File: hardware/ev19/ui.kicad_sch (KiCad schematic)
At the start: 43 parts, among them CN3 BM14B(0.8)-24DS-0.4V(53), J14 Conn_01x18_MountingPin, Q5 2N7002, SW4 SW_Push, SW5 SW_Push, SW6 SW_Push, SW7 SW_Push, U10 STM32F405RGTx

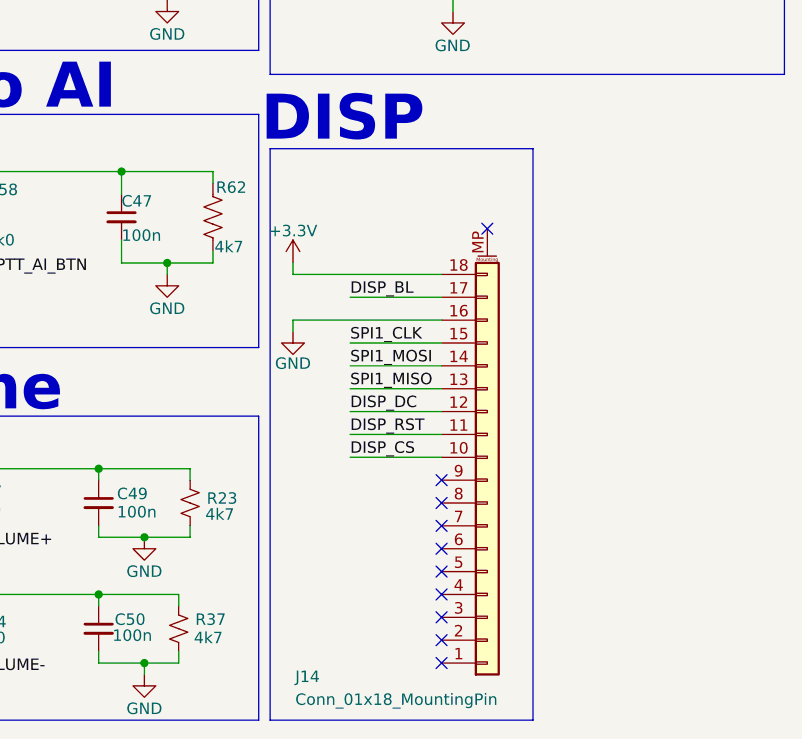
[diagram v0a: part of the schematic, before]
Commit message: wip- laid out the analog power section, added screen cut outs, decided on positions
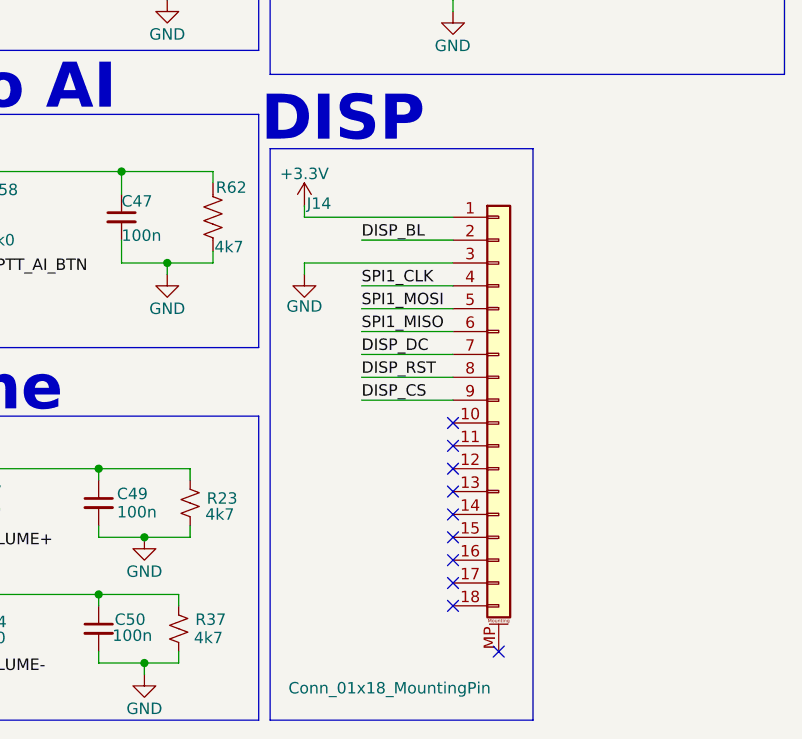
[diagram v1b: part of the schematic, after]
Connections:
- net +3.3V: now also J14.1 (Pin_1); no longer J14.18 (Pin_18)
- net DISP_BL: now also J14.2 (Pin_2); no longer J14.17 (Pin_17)
- net DISP_CS: now also J14.9 (Pin_9); no longer J14.10 (Pin_10)
- net DISP_DC: now also J14.7 (Pin_7); no longer J14.12 (Pin_12)
- net DISP_RST: now also J14.8 (Pin_8); no longer J14.11 (Pin_11)
- net GND: now also J14.3 (Pin_3); no longer J14.16 (Pin_16)
- net SPI1_CLK: now also J14.4 (Pin_4); no longer J14.15 (Pin_15)
- net SPI1_MISO: now also J14.6 (Pin_6); no longer J14.13 (Pin_13)
- net SPI1_MOSI: now also J14.5 (Pin_5); no longer J14.14 (Pin_14)
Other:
- moved on the sheet: J14
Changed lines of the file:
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@@
 	)
 	(no_connect
-		(at 245.11 147.32)
+		(at 246.38 140.97)
 	)
 	(no_connect
-		(at 245.11 142.24)
+		(at 246.38 135.89)
 	)
 	(no_connect
-		(at 245.11 139.7)
+		(at 246.38 133.35)
 	)
 	(no_connect
@@
 	)
 	(no_connect
-		(at 250.19 109.22)
+		(at 251.46 156.21)
 	)
 	(no_connect
-		(at 245.11 157.48)
+		(at 246.38 151.13)
 	)
 	(no_connect
-		(at 245.11 154.94)
+		(at 246.38 148.59)
 	)
 	(no_connect
-		(at 245.11 152.4)
+		(at 246.38 146.05)
 	)
 	(no_connect
-		(at 245.11 144.78)
+		(at 246.38 138.43)
 	)
 	(no_connect
@@
 	)
 	(no_connect
-		(at 245.11 137.16)
+		(at 246.38 130.81)
 	)
 	(no_connect
-		(at 245.11 149.86)
+		(at 246.38 143.51)
 	)
 	(wire
@@
 	(wire
 		(pts
-			(xy 234.95 121.92) (xy 245.11 121.92)
+			(xy 236.22 115.57) (xy 246.38 115.57)
 		)
 		(stroke
@@
 	(wire
 		(pts
-			(xy 228.6 119.38) (xy 245.11 119.38)
+			(xy 229.87 113.03) (xy 246.38 113.03)
 		)
 		(stroke
@@
 	(wire
 		(pts
-			(xy 234.95 132.08) (xy 245.11 132.08)
+			(xy 236.22 125.73) (xy 246.38 125.73)
 		)
 		(stroke
@@
 	(wire
 		(pts
-			(xy 228.6 113.03) (xy 228.6 114.3)
+			(xy 229.87 106.68) (xy 229.87 107.95)
 		)
 		(stroke
@@
 	(wire
 		(pts
-			(xy 228.6 120.65) (xy 228.6 119.38)
+			(xy 229.87 114.3) (xy 229.87 113.03)
 		)
 		(stroke
@@
 	(wire
 		(pts
-			(xy 234.95 134.62) (xy 245.11 134.62)
+			(xy 236.22 128.27) (xy 246.38 128.27)
 		)
 		(stroke
@@
 	(wire
 		(pts
-			(xy 234.95 129.54) (xy 245.11 129.54)
+			(xy 236.22 123.19) (xy 246.38 123.19)
 		)
 		(stroke
@@
 	(wire
 		(pts
-			(xy 228.6 114.3) (xy 245.11 114.3)
+			(xy 229.87 107.95) (xy 246.38 107.95)
 		)
 		(stroke
@@
 	(wire
 		(pts
-			(xy 234.95 116.84) (xy 245.11 116.84)
+			(xy 236.22 110.49) (xy 246.38 110.49)
 		)
 		(stroke
@@
 	(wire
 		(pts
-			(xy 234.95 127) (xy 245.11 127)
+			(xy 236.22 120.65) (xy 246.38 120.65)
 		)
 		(stroke
@@
 	(wire
 		(pts
-			(xy 234.95 124.46) (xy 245.11 124.46)
+			(xy 236.22 118.11) (xy 246.38 118.11)
 		)
 		(stroke
@@
 	)
 	(label "SPI1_MISO"
-		(at 234.95 127 0)
+		(at 236.22 120.65 0)
 		(effects
 			(font
@@
 	)
 	(label "DISP_CS"
-		(at 234.95 134.62 0)
+		(at 236.22 128.27 0)
 		(effects
 			(font
@@
 	)
 	(label "SPI1_MOSI"
-		(at 234.95 124.46 0)
+		(at 236.22 118.11 0)
 		(effects
 			(font
@@
 	)
 	(label "DISP_DC"
-		(at 234.95 129.54 0)
+		(at 236.22 123.19 0)
 		(effects
 			(font
@@
 	)
 	(label "DISP_RST"
-		(at 234.95 132.08 0)
+		(at 236.22 125.73 0)
 		(effects
 			(font
@@
 	)
 	(label "SPI1_CLK"
-		(at 234.95 121.92 0)
+		(at 236.22 115.57 0)
 		(effects
 			(font
@@
 	)
 	(label "DISP_BL"
-		(at 234.95 116.84 0)
+		(at 236.22 110.49 0)
 		(effects
 			(font
@@
 	(symbol
 		(lib_id "power:GND")
-		(at 228.6 120.65 0)
+		(at 229.87 114.3 0)
 		(unit 1)
 		(body_style 1)
@@
 		(dnp no)
 		(property "Reference" "#PWR0109"
-			(at 228.6 127 0)
+			(at 229.87 120.65 0)
 			(hide yes)
 			(show_name no)
@@
 		)
 		(property "Value" "GND"
-			(at 228.6 124.206 0)
+			(at 229.87 117.856 0)
 			(show_name no)
 			(do_not_autoplace no)
@@
 		)
 		(property "Footprint" ""
-			(at 228.6 120.65 0)
+			(at 229.87 114.3 0)
 			(hide yes)
 			(show_name no)
@@
 		)
 		(property "Datasheet" ""
-			(at 228.6 120.65 0)
+			(at 229.87 114.3 0)
 			(hide yes)
 			(show_name no)
@@
 		)
 		(property "Description" "Power symbol creates a global label with name \"GND\" , ground"
-			(at 228.6 120.65 0)
+			(at 229.87 114.3 0)
 			(hide yes)
 			(show_name no)
@@
 	(symbol
 		(lib_id "Connector_Generic_MountingPin:Conn_01x18_MountingPin")
-		(at 250.19 137.16 0)
-		(mirror x)
+		(at 251.46 128.27 0)
 		(unit 1)
 		(body_style 1)
@@
 		(dnp no)
 		(property "Reference" "J14"
-			(at 228.854 159.004 0)
+			(at 230.124 106.426 0)
 			(show_name no)
 			(do_not_autoplace no)
@@
 		)
 		(property "Value" "Conn_01x18_MountingPin"
-			(at 228.854 161.544 0)
+			(at 228.092 160.274 0)
 			(show_name no)
 			(do_not_autoplace no)
@@
 		)
 		(property "Footprint" "Connector_FFC-FPC:Hirose_FH12-18S-0.5SH_1x18-1MP_P0.50mm_Horizontal"
-			(at 250.19 137.16 0)
+			(at 251.46 128.27 0)
 			(hide yes)
 			(show_name no)
@@
 		)
 		(property "Datasheet" ""
-			(at 250.19 137.16 0)
+			(at 251.46 128.27 0)
 			(hide yes)
 			(show_name no)
@@
 		)
 		(property "Description" "Generic connectable mounting pin connector, single row, 01x18, script generated (kicad-library-utils/schlib/autogen/connector/)"
-			(at 250.19 137.16 0)
+			(at 251.46 128.27 0)
 			(hide yes)
 			(show_name no)
@@
 		)
 		(property "JLCPCB Part #" "C2856802"
-			(at 250.19 137.16 0)
+			(at 251.46 128.27 0)
 			(hide yes)
 			(show_name no)
@@
 	(symbol
 		(lib_id "power:+3.3V")
-		(at 228.6 113.03 0)
+		(at 229.87 106.68 0)
 		(unit 1)
 		(body_style 1)
@@
 		(dnp no)
 		(property "Reference" "#PWR0108"
-			(at 228.6 116.84 0)
+			(at 229.87 110.49 0)
 			(hide yes)
 			(show_name no)
@@
 		)
 		(property "Value" "+3.3V"
-			(at 228.6 109.474 0)
+			(at 229.87 103.124 0)
 			(show_name no)
 			(do_not_autoplace no)
@@
 		)
 		(property "Footprint" ""
-			(at 228.6 113.03 0)
+			(at 229.87 106.68 0)
 			(hide yes)
 			(show_name no)
@@
 		)
 		(property "Datasheet" ""
-			(at 228.6 113.03 0)
+			(at 229.87 106.68 0)
 			(hide yes)
 			(show_name no)
@@
 		)
 		(property "Description" "Power symbol creates a global label with name \"+3.3V\""
-			(at 228.6 113.03 0)
+			(at 229.87 106.68 0)
 			(hide yes)
 			(show_name no)

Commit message: Laid out all high speed lines, created gnda, 3.0va, and dgnd 3.3vd in analog sections
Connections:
- net MIC_IO renamed MIC_PTT_BTN
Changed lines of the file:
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@@
-	(wire
-		(pts
-			(xy 73.66 54.61) (xy 87.63 54.61)
-		)
-		(stroke
-			(width 0)
-			(type default)
-		)
-	)
 	(wire
 		(pts
@@
 		(pts
 			(xy 191.77 158.75) (xy 191.77 156.21)
+		)
+		(stroke
+			(width 0)
+			(type default)
+		)
+	)
+	(wire
+		(pts
+			(xy 46.99 54.61) (xy 87.63 54.61)
 		)
 		(stroke
@@
 	(label "SPI1_CLK"
 		(at 73.66 57.15 0)
-		(effects
-			(font
-				(size 1.27 1.27)
-			)
-			(justify left bottom)
-		)
-	)
-	(label "MIC_IO"
-		(at 73.66 54.61 0)
 		(effects
 			(font
@@
 		(effects
 			(font
+				(size 1.27 1.27)
+			)
+			(justify right)
+		)
+	)
+	(hierarchical_label "MIC_PTT_BTN"
+		(shape input)
+		(at 46.99 54.61 180)
+		(effects
+			(font

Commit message: Change connector for display, but will need to change footprint
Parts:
- removed J14: Conn_01x18_MountingPin, Connector_FFC-FPC:Hirose_FH12-18S-0.5SH_1x18-1MP_P0.50mm_Horizontal, symbol Connector_Generic_MountingPin:Conn_01x18_MountingPin
- added J13: Conn_01x08_Pin, Connector_PinHeader_2.54mm:PinHeader_1x08_P2.54mm_Vertical_SMD_Pin1Left, symbol Connector:Conn_01x08_Pin
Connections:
- net +3.3V: now also J13.8 (Pin_8)
- net DISP_BL: now also J13.1 (Pin_1)
- net DISP_CS: now also J13.4 (Pin_4)
- net DISP_DC: now also J13.3 (Pin_3)
- net DISP_RST: now also J13.2 (Pin_2)
- net GND: now also J13.7 (Pin_7)
- net SPI1_CLK: now also J13.5 (Pin_5)
- net SPI1_MOSI: now also J13.6 (Pin_6)
- no-connect marks 12 -> 2
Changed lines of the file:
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@@
 	)
 	(no_connect
-		(at 246.38 140.97)
-	)
-	(no_connect
-		(at 246.38 135.89)
-	)
-	(no_connect
-		(at 246.38 133.35)
-	)
-	(no_connect
 		(at 245.11 40.64)
 	)
 	(no_connect
-		(at 251.46 156.21)
-	)
-	(no_connect
-		(at 246.38 151.13)
-	)
-	(no_connect
-		(at 246.38 148.59)
-	)
-	(no_connect
-		(at 246.38 146.05)
-	)
-	(no_connect
-		(at 246.38 138.43)
-	)
-	(no_connect
 		(at 128.27 57.15)
 	)
-	(no_connect
-		(at 246.38 130.81)
-	)
-	(no_connect
-		(at 246.38 143.51)
-	)
 	(wire
 		(pts
@@
 	(wire
 		(pts
-			(xy 229.87 113.03) (xy 246.38 113.03)
+			(xy 229.87 110.49) (xy 246.38 110.49)
 		)
 		(stroke
@@
 	(wire
 		(pts
-			(xy 236.22 125.73) (xy 246.38 125.73)
+			(xy 236.22 123.19) (xy 246.38 123.19)
 		)
 		(stroke
@@
 	(wire
 		(pts
-			(xy 229.87 114.3) (xy 229.87 113.03)
+			(xy 229.87 111.76) (xy 229.87 110.49)
 		)
 		(stroke
@@
 	(wire
 		(pts
-			(xy 236.22 128.27) (xy 246.38 128.27)
+			(xy 236.22 118.11) (xy 246.38 118.11)
 		)
 		(stroke
@@
 	(wire
 		(pts
-			(xy 236.22 123.19) (xy 246.38 123.19)
+			(xy 236.22 120.65) (xy 246.38 120.65)
 		)
 		(stroke
@@
 	(wire
 		(pts
-			(xy 236.22 110.49) (xy 246.38 110.49)
+			(xy 236.22 125.73) (xy 246.38 125.73)
 		)
 		(stroke
@@
 	(wire
 		(pts
-			(xy 236.22 120.65) (xy 246.38 120.65)
-		)
-		(stroke
-			(width 0)
-			(type default)
-		)
-	)
-	(wire
-		(pts
 			(xy 128.27 92.71) (xy 160.02 92.71)
 		)
@@
 	(wire
 		(pts
-			(xy 236.22 118.11) (xy 246.38 118.11)
+			(xy 236.22 113.03) (xy 246.38 113.03)
 		)
 		(stroke
@@
 		)
 	)
-	(label "SPI1_MISO"
-		(at 236.22 120.65 0)
-		(effects
-			(font
-				(size 1.27 1.27)
-			)
-			(justify left bottom)
-		)
-	)
 	(label "SPI1_MOSI"
 		(at 73.66 62.23 0)
@@
 	)
 	(label "DISP_CS"
-		(at 236.22 128.27 0)
+		(at 236.22 118.11 0)
 		(effects
 			(font
@@
 	)
 	(label "SPI1_MOSI"
-		(at 236.22 118.11 0)
+		(at 236.22 113.03 0)
 		(effects
 			(font
@@
 	)
 	(label "DISP_DC"
-		(at 236.22 123.19 0)
+		(at 236.22 120.65 0)
 		(effects
 			(font
@@
 	)
 	(label "DISP_RST"
-		(at 236.22 125.73 0)
+		(at 236.22 123.19 0)
 		(effects
 			(font
@@
 	)
 	(label "DISP_BL"
-		(at 236.22 110.49 0)
+		(at 236.22 125.73 0)
 		(effects
 			(font
@@
 	(symbol
 		(lib_id "power:GND")
-		(at 229.87 114.3 0)
+		(at 229.87 111.76 0)
 		(unit 1)
 		(body_style 1)
@@
 		(dnp no)
 		(property "Reference" "#PWR0109"
-			(at 229.87 120.65 0)
+			(at 229.87 118.11 0)
 			(hide yes)
 			(show_name no)
@@
 		)
 		(property "Value" "GND"
-			(at 229.87 117.856 0)
+			(at 229.87 115.316 0)
 			(show_name no)
 			(do_not_autoplace no)
@@
 		)
 		(property "Footprint" ""
-			(at 229.87 114.3 0)
+			(at 229.87 111.76 0)
 			(hide yes)
 			(show_name no)
@@
 		)
 		(property "Datasheet" ""
-			(at 229.87 114.3 0)
+			(at 229.87 111.76 0)
 			(hide yes)
 			(show_name no)
@@
 		)
 		(property "Description" "Power symbol creates a global label with name \"GND\" , ground"
-			(at 229.87 114.3 0)
+			(at 229.87 111.76 0)
 			(hide yes)
 			(show_name no)
@@
 	)
 	(symbol
-		(lib_id "Connector_Generic_MountingPin:Conn_01x18_MountingPin")
-		(at 251.46 128.27 0)
-		(unit 1)
-		(body_style 1)
-		(exclude_from_sim no)
-		(in_bom yes)
-		(on_board yes)
-		(in_pos_files yes)
-		(dnp no)
-		(property "Reference" "J14"
-			(at 230.124 106.426 0)
-			(show_name no)
-			(do_not_autoplace no)
-			(effects
-				(font
-					(size 1.27 1.27)
-				)
-				(justify left)
-			)
-		)
-		(property "Value" "Conn_01x18_MountingPin"
-			(at 228.092 160.274 0)
-			(show_name no)
-			(do_not_autoplace no)
-			(effects
-				(font
-					(size 1.27 1.27)
-				)
-				(justify left)
-			)
-		)
-		(property "Footprint" "Connector_FFC-FPC:Hirose_FH12-18S-0.5SH_1x18-1MP_P0.50mm_Horizontal"
-			(at 251.46 128.27 0)
-			(hide yes)
-			(show_name no)
-			(do_not_autoplace no)
-			(effects
-				(font
-					(size 1.27 1.27)
-				)
-			)
-		)
-		(property "Datasheet" ""
-			(at 251.46 128.27 0)
-			(hide yes)
-			(show_name no)
-			(do_not_autoplace no)
-			(effects
-				(font
-					(size 1.27 1.27)
-				)
-			)
-		)
-		(property "Description" "Generic connectable mounting pin connector, single row, 01x18, script generated (kicad-library-utils/schlib/autogen/connector/)"
-			(at 251.46 128.27 0)
-			(hide yes)
-			(show_name no)
-			(do_not_autoplace no)
-			(effects
-				(font
-					(size 1.27 1.27)
-				)
-			)
-		)
-		(property "JLCPCB Part #" "C2856802"
-			(at 251.46 128.27 0)
-			(hide yes)
-			(show_name no)
-			(do_not_autoplace no)
-			(effects
-				(font
-					(size 1.27 1.27)
-				)
-			)
-		)
-		(pin "8"
-		)
-		(pin "13"
-		)
-		(pin "15"
-		)
-		(pin "17"
-		)
-		(pin "14"
-		)
-		(pin "3"
-		)
-		(pin "4"
-		)
-		(pin "5"
-		)
-		(pin "6"
-		)
-		(pin "1"
-		)
-		(pin "18"
-		)
-		(pin "9"
-		)
-		(pin "2"
-		)
-		(pin "10"
-		)
-		(pin "11"
-		)
-		(pin "12"
-		)
-		(pin "MP"
-		)
-		(pin "7"
-		)
-		(pin "16"
-		)
-		(instances
-			(project "ev19"
-				(path "/bd865368-262b-4f76-b7a6-1673c2cb0f8c/3dc257c8-f72f-473f-bf23-b8869158b2ba"
-					(reference "J14")
-					(unit 1)
-				)
-			)
-		)
-	)
-	(symbol
 		(lib_id "Device:R_US")
 		(at 219.71 107.95 180)
@@
 					(unit 1)
 				)
+			)
+		)
+	)
+	(symbol
+		(lib_id "Connector:Conn_01x08_Pin")
+		(at 251.46 118.11 180)
+		(unit 1)
+		(body_style 1)
+		(exclude_from_sim no)
+		(in_bom yes)
+		(on_board yes)
+		(in_pos_files yes)
+		(dnp no)
+		(property "Reference" "J13"
+			(at 237.744 105.664 0)
+			(show_name no)
+			(do_not_autoplace no)
+			(effects
+				(font
+					(size 1.27 1.27)
+				)
+				(justify right)
+			)
+		)
+		(property "Value" "Conn_01x08_Pin"
+			(at 237.49 103.378 0)
+			(show_name no)
+			(do_not_autoplace no)
+			(effects
+				(font
+					(size 1.27 1.27)
+				)
+				(justify right)
+			)
+		)
+		(property "Footprint" "Connector_PinHeader_2.54mm:PinHeader_1x08_P2.54mm_Vertical_SMD_Pin1Left"
+			(at 251.46 118.11 0)
+			(hide yes)
+			(show_name no)
+			(do_not_autoplace no)
+			(effects
+				(font
+					(size 1.27 1.27)
+				)
+			)
+		)
+		(property "Datasheet" ""
+			(at 251.46 118.11 0)
+			(hide yes)
+			(show_name no)
+			(do_not_autoplace no)
+			(effects
+				(font
+					(size 1.27 1.27)
+				)
+			)
+		)
+		(property "Description" "Generic connector, single row, 01x08, script generated"
+			(at 251.46 118.11 0)
+			(hide yes)
+			(show_name no)
+			(do_not_autoplace no)
+			(effects
+				(font
+					(size 1.27 1.27)
+				)
+			)
+		)
+		(pin "3"
+		)
+		(pin "5"
+		)
+		(pin "2"
+		)
+		(pin "4"
+		)
+		(pin "1"
+		)
+		(pin "6"
+		)
+		(pin "7"
+		)
+		(pin "8"
+		)
+		(instances
+			(project "ev19"
+				(path "/bd865368-262b-4f76-b7a6-1673c2cb0f8c/3dc257c8-f72f-473f-bf23-b8869158b2ba"
+					(reference "J13")
+					(unit 1)
+				)
